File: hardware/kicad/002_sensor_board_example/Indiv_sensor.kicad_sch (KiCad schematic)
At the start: 5 parts, among them Q301 AO3400A, U301 VCNT2025X01

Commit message: 002 sensor board: 5V bus rework, library consolidation, DRC pass
Board (002):
- Remove SS14 bridging diode; USB-C VBUS and JST V+ are now one net.
  Worst case is back-powering a host's VBUS, acceptable in a uniform
  5V fleet, and it drops 185mW in the bridging case.
- Remove the 8x 47k CS pull-ups. At 47k they parked the TLA2518 CS
  inputs mid-rail (1.7-2.1V, between VIL 0.99 and VIH 2.31); the
  internal pull-down now defines them cleanly low. Firmware must drive
  CS high before configuring SPI.
- 5V pour along the bottom edge, 3.3V moved up to the mounting rail.
- USB-C relocated; ~200mm D+/D- run on F.Cu over the B.Cu GND pour.
- Screw-head keepouts on all mounting holes.
- Board grown 2mm in Y -> 413.66 x 35.00 mm.

Net classes:
- USB_DIFF_90 -> USB_FS, diff pair 0.8/0.15 -> 0.35/0.15. The old name
  claimed 90 ohm; on a 1.51mm 2-layer stackup it is ~140 ohm and cannot
  be otherwise. Irrelevant at Full Speed.
- Add PWR_5V (+5V) and RS485 (/RS485_P, /RS485_N).
- Restore the +3V3 -> VCC assignment lost during the rename.

Libraries:
- footprints/ -> footprints.pretty/ so KiCad will save into it.
- Consolidate symbols into PHOTON / PHOTON_Modified on 001d and 002;
  drop unused vendor-exported libraries.
- Add mousebite_34mm: 17x 1.2mm NPTH at 2mm pitch. 0.8mm webs cut more
  easily than the old 1.4mm and still pass a 0.3mm trace.
- Fix MountingHole_2.7mm_M2.5_Keepout: it disallowed pads, so each hole
  flagged its own NPTH (17 DRC errors).

Fab outputs now tracked via .gitignore negation for production/*.csv.

Co-Authored-By: Claude Opus 5 <noreply@anthropic.com>
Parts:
- U301: symbol VCNT2020:VCNT2020 -> PHOTON:VCNT2020
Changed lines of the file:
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@@
 	)
 	(symbol
+		(lib_name "+3V3_1")
 		(lib_id "power:+3V3")
 		(at 130.81 80.01 0)
@@
 	)
 	(symbol
-		(lib_id "VCNT2020:VCNT2020")
+		(lib_id "PHOTON:VCNT2020")
 		(at 138.43 97.79 0)
 		(unit 1)

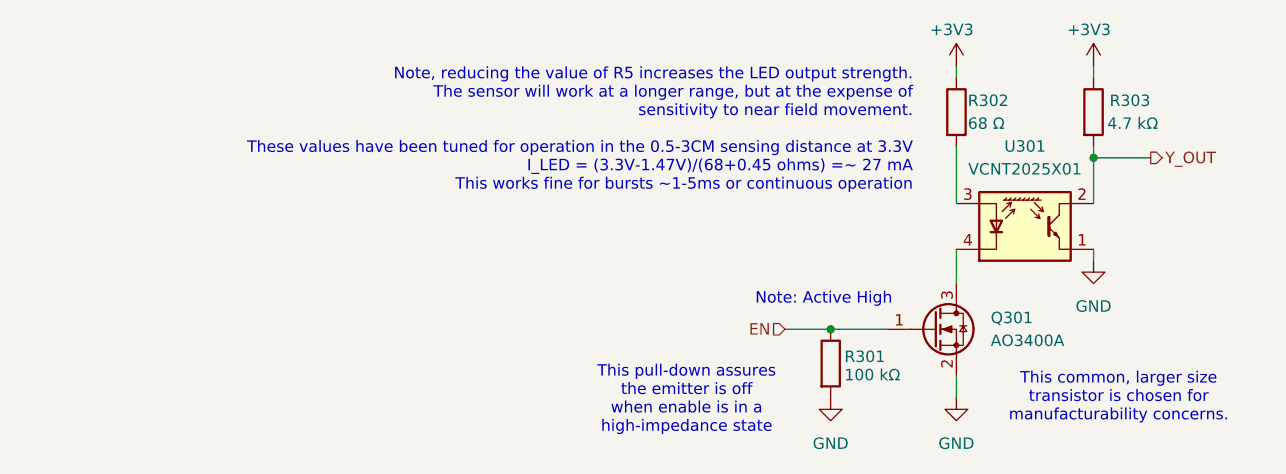
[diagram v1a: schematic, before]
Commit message: 002: ERC/DRC to zero, symbol and value cleanup
Schematic (ERC 24 -> 0):
- VCNT2020 renamed to VCNT2025X01, matching the part actually fitted.
  Pin types preserved: passive / open_collector / passive / passive.
  The old auto-generated VCNT2025X01 symbol (all pins Unspecified) is gone.
- THVD1424RGTR: 10 pins off Unspecified (R, RE, DE, D, TERM_TX, TERM_RX,
  Y, Z, VIO, H/F). VIO was typed as a signal despite being a supply pin.
- TLA2518IRTER: DECAP -> Passive, clearing 8 warnings at once.
- PWR_FLAG moved off J3's VBUS (which J3 already drives as a Power output)
  onto GND, which had none. One move, two errors.
- JP1/JP2/JP4 repointed to stock Jumper:SolderJumper_2_Open. The project
  copy was KiCad's older stock symbol, not a deliberate modification.
- R1 1M -> 0 ohm, bonding the USB-C shell to GND. A lone 1M is a static
  bleed, not a shield connection: open at every frequency that matters,
  and it isolated nothing since J3's GND pins are already bonded.

Layout:
- MountingHole keepout had (pads not_allowed), so each hole flagged its
  own NPTH. Fixed and patched into all 17 instances.
- Mousebite silkscreen removed (library + all 3 placements). The dashed
  line crossed the pours end to end and caused ~61 of the DRC warnings.
- 30 duplicate vias deleted. Each pair was 1 nm apart from a float->int
  round-trip in the layout plugin, so KiCad's "delete redundant vias"
  could not see them while DRC's co-located check could.
- min_resolved_spokes 2 -> 1; single-spoke pads are accepted on this
  board rather than excluded per-violation.

BOM hygiene:
- Component values normalised: no space before units, ASCII u instead of
  U+03BC, and 3.3u given its missing unit. Merges 100 kohm/100kohm and
  1 uF/1uF, which would otherwise export as separate lines for identical
  parts. 181 edits across schematics and PCB, kept in sync.

Libraries:
- PHOTON_Modified reduced to the two symbols that genuinely diverge from
  stock: Crystal_GND24 and USB_C_Receptacle_USB2.0.

Known o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
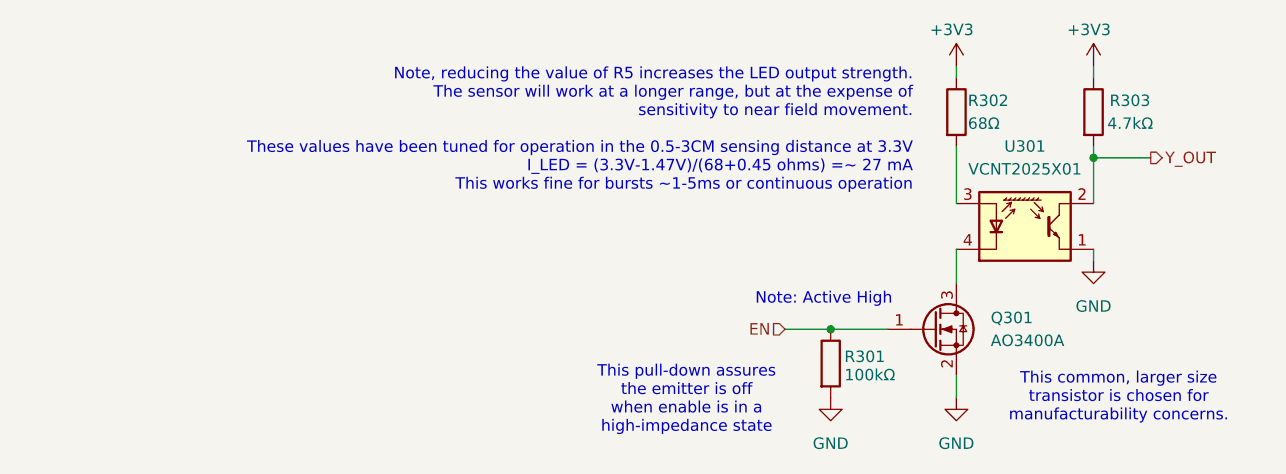
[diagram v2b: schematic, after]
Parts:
- R301: value 100 kΩ -> 100kΩ
- R302: value 68 Ω -> 68Ω
- R303: value 4.7 kΩ -> 4.7kΩ
- U301: symbol PHOTON:VCNT2020 -> PHOTON:VCNT2025X01; JLCPCB Part # (none) -> C7431257
